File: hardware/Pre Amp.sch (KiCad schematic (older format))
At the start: 19 parts

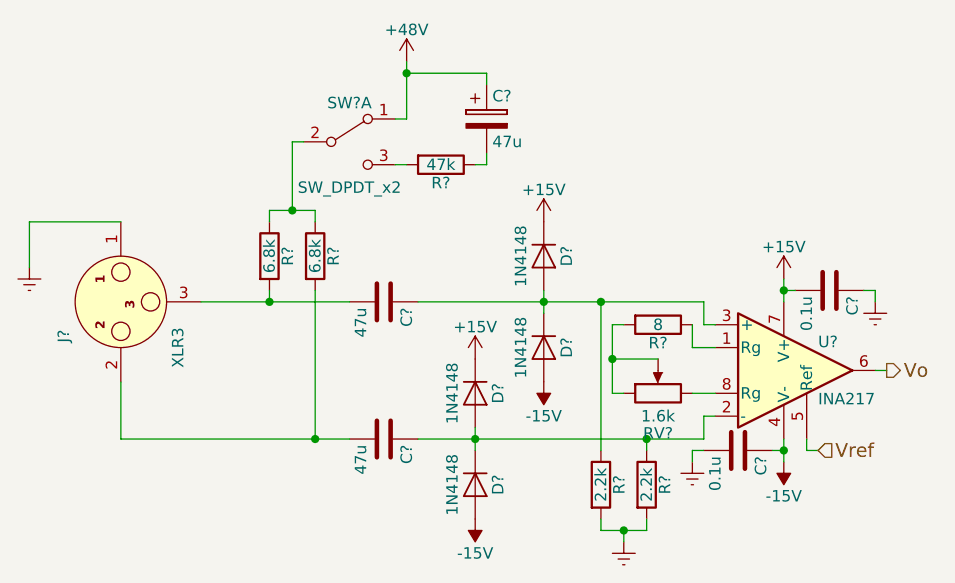
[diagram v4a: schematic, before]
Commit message: Began stm32 power wiring
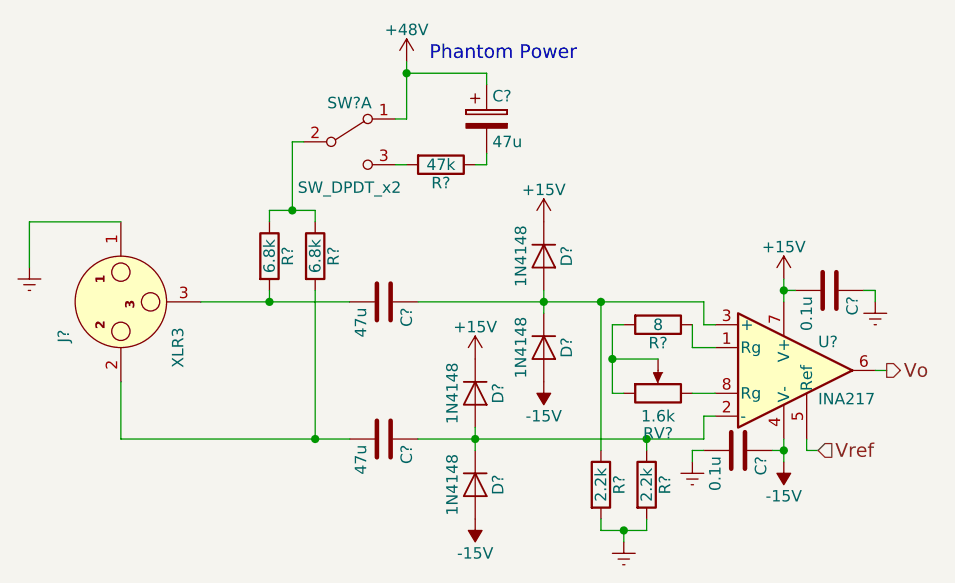
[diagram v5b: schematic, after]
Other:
- note added: "Phantom Power"
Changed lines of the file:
@@
 $Descr A4 11693 8268
 encoding utf-8
-Sheet 3 5
+Sheet 2 5
 Title ""
 Date ""
@@
 $EndComp
 $Comp
-L Earth #PWR013
+L Earth #PWR019
 U 1 1 595B230E
 P 2350 2400
-AR Path="/595B226C/595B230E" Ref="#PWR013"  Part="1"
-AR Path="/595BE132/595B230E" Ref="#PWR021"  Part="1"
-AR Path="/595BEAC4/595B230E" Ref="#PWR029"  Part="1"
-AR Path="/595BEACA/595B230E" Ref="#PWR037"  Part="1"
-F 0 "#PWR037" H 2350 2150 50  0001 C CNN
+AR Path="/595B226C/595B230E" Ref="#PWR019"  Part="1"
+AR Path="/595BE132/595B230E" Ref="#PWR027"  Part="1"
+AR Path="/595BEAC4/595B230E" Ref="#PWR035"  Part="1"
+AR Path="/595BEACA/595B230E" Ref="#PWR043"  Part="1"
+F 0 "#PWR043" H 2350 2150 50  0001 C CNN
 F 1 "Earth" H 2350 2250 50  0001 C CNN
 F 2 "" H 2350 2400 50  0001 C CNN
@@
 Connection ~ 4600 2550
 $Comp
-L +15V #PWR014
+L +15V #PWR020
 U 1 1 595B298D
 P 4300 2800
-AR Path="/595B226C/595B298D" Ref="#PWR014"  Part="1"
-AR Path="/595BE132/595B298D" Ref="#PWR022"  Part="1"
-AR Path="/595BEAC4/595B298D" Ref="#PWR030"  Part="1"
-AR Path="/595BEACA/595B298D" Ref="#PWR038"  Part="1"
-F 0 "#PWR038" H 4300 2650 50  0001 C CNN
+AR Path="/595B226C/595B298D" Ref="#PWR020"  Part="1"
+AR Path="/595BE132/595B298D" Ref="#PWR028"  Part="1"
+AR Path="/595BEAC4/595B298D" Ref="#PWR036"  Part="1"
+AR Path="/595BEACA/595B298D" Ref="#PWR044"  Part="1"
+F 0 "#PWR044" H 4300 2650 50  0001 C CNN
 F 1 "+15V" H 4300 2940 50  0000 C CNN
 F 2 "" H 4300 2800 50  0001 C CNN
@@
 $EndComp
 $Comp
-L +15V #PWR015
+L +15V #PWR021
 U 1 1 595B29D8
 P 4600 2200
-AR Path="/595B226C/595B29D8" Ref="#PWR015"  Part="1"
-AR Path="/595BE132/595B29D8" Ref="#PWR023"  Part="1"
-AR Path="/595BEAC4/595B29D8" Ref="#PWR031"  Part="1"
-AR Path="/595BEACA/595B29D8" Ref="#PWR039"  Part="1"
-F 0 "#PWR039" H 4600 2050 50  0001 C CNN
+AR Path="/595B226C/595B29D8" Ref="#PWR021"  Part="1"
+AR Path="/595BE132/595B29D8" Ref="#PWR029"  Part="1"
+AR Path="/595BEAC4/595B29D8" Ref="#PWR037"  Part="1"
+AR Path="/595BEACA/595B29D8" Ref="#PWR045"  Part="1"
+F 0 "#PWR045" H 4600 2050 50  0001 C CNN
 F 1 "+15V" H 4600 2340 50  0000 C CNN
 F 2 "" H 4600 2200 50  0001 C CNN
@@
 	5050 3550 5050 3500
 $Comp
-L Earth #PWR016
+L Earth #PWR022
 U 1 1 595B304F
 P 4950 3600
-AR Path="/595B226C/595B304F" Ref="#PWR016"  Part="1"
-AR Path="/595BE132/595B304F" Ref="#PWR024"  Part="1"
-AR Path="/595BEAC4/595B304F" Ref="#PWR032"  Part="1"
-AR Path="/595BEACA/595B304F" Ref="#PWR040"  Part="1"
-F 0 "#PWR040" H 4950 3350 50  0001 C CNN
+AR Path="/595B226C/595B304F" Ref="#PWR022"  Part="1"
+AR Path="/595BE132/595B304F" Ref="#PWR030"  Part="1"
+AR Path="/595BEAC4/595B304F" Ref="#PWR038"  Part="1"
+AR Path="/595BEACA/595B304F" Ref="#PWR046"  Part="1"
+F 0 "#PWR046" H 4950 3350 50  0001 C CNN
 F 1 "Earth" H 4950 3450 50  0001 C CNN
 F 2 "" H 4950 3600 50  0001 C CNN
@@
 	5250 2750 5350 2750
 $Comp
-L +15V #PWR017
+L +15V #PWR023
 U 1 1 595B3F8A
 P 5650 2450
-AR Path="/595B226C/595B3F8A" Ref="#PWR017"  Part="1"
-AR Path="/595BE132/595B3F8A" Ref="#PWR025"  Part="1"
-AR Path="/595BEAC4/595B3F8A" Ref="#PWR033"  Part="1"
-AR Path="/595BEACA/595B3F8A" Ref="#PWR041"  Part="1"
-F 0 "#PWR041" H 5650 2300 50  0001 C CNN
+AR Path="/595B226C/595B3F8A" Ref="#PWR023"  Part="1"
+AR Path="/595BE132/595B3F8A" Ref="#PWR031"  Part="1"
+AR Path="/595BEAC4/595B3F8A" Ref="#PWR039"  Part="1"
+AR Path="/595BEACA/595B3F8A" Ref="#PWR047"  Part="1"
+F 0 "#PWR047" H 5650 2300 50  0001 C CNN
 F 1 "+15V" H 5650 2590 50  0000 C CNN
 F 2 "" H 5650 2450 50  0001 C CNN
@@
 $EndComp
 $Comp
-L Earth #PWR018
+L Earth #PWR024
 U 1 1 595B4161
 P 5250 3250
-AR Path="/595B226C/595B4161" Ref="#PWR018"  Part="1"
-AR Path="/595BE132/595B4161" Ref="#PWR026"  Part="1"
-AR Path="/595BEAC4/595B4161" Ref="#PWR034"  Part="1"
-AR Path="/595BEACA/595B4161" Ref="#PWR042"  Part="1"
-F 0 "#PWR042" H 5250 3000 50  0001 C CNN
+AR Path="/595B226C/595B4161" Ref="#PWR024"  Part="1"
+AR Path="/595BE132/595B4161" Ref="#PWR032"  Part="1"
+AR Path="/595BEAC4/595B4161" Ref="#PWR040"  Part="1"
+AR Path="/595BEACA/595B4161" Ref="#PWR048"  Part="1"
+F 0 "#PWR048" H 5250 3000 50  0001 C CNN
 F 1 "Earth" H 5250 3100 50  0001 C CNN
 F 2 "" H 5250 3250 50  0001 C CNN
@@
 $EndComp
 $Comp
-L Earth #PWR019
+L Earth #PWR025
 U 1 1 595B4196
 P 6050 2550
-AR Path="/595B226C/595B4196" Ref="#PWR019"  Part="1"
-AR Path="/595BE132/595B4196" Ref="#PWR027"  Part="1"
-AR Path="/595BEAC4/595B4196" Ref="#PWR035"  Part="1"
-AR Path="/595BEACA/595B4196" Ref="#PWR043"  Part="1"
-F 0 "#PWR043" H 6050 2300 50  0001 C CNN
+AR Path="/595B226C/595B4196" Ref="#PWR025"  Part="1"
+AR Path="/595BE132/595B4196" Ref="#PWR033"  Part="1"
+AR Path="/595BEAC4/595B4196" Ref="#PWR041"  Part="1"
+AR Path="/595BEACA/595B4196" Ref="#PWR049"  Part="1"
+F 0 "#PWR049" H 6050 2300 50  0001 C CNN
 F 1 "Earth" H 6050 2400 50  0001 C CNN
 F 2 "" H 6050 2550 50  0001 C CNN
@@
 $EndComp
 $Comp
-L +48V #PWR020
+L +48V #PWR026
 U 1 1 595B49A0
 P 4000 1500
-AR Path="/595B226C/595B49A0" Ref="#PWR020"  Part="1"
-AR Path="/595BE132/595B49A0" Ref="#PWR028"  Part="1"
-AR Path="/595BEAC4/595B49A0" Ref="#PWR036"  Part="1"
-AR Path="/595BEACA/595B49A0" Ref="#PWR044"  Part="1"
-F 0 "#PWR044" H 4000 1350 50  0001 C CNN
+AR Path="/595B226C/595B49A0" Ref="#PWR026"  Part="1"
+AR Path="/595BE132/595B49A0" Ref="#PWR034"  Part="1"
+AR Path="/595BEAC4/595B49A0" Ref="#PWR042"  Part="1"
+AR Path="/595BEACA/595B49A0" Ref="#PWR050"  Part="1"
+F 0 "#PWR050" H 4000 1350 50  0001 C CNN
 F 1 "+48V" H 4000 1640 50  0000 C CNN
 F 2 "" H 4000 1500 50  0001 C CNN
@@
 Wire Wire Line
 	6100 2850 6050 2850
+Text Notes 4100 1500 0    60   ~ 0
+Phantom Power
 $EndSCHEMATC
